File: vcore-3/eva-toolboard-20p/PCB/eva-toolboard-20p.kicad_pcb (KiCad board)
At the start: 2 copper layers, 44.1 x 48.8 mm, 12 parts, among them J4 Main connector

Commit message: Added totally useless but cute logos
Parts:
- added svg2mod: G***, logos:EVA_Logo, F.Cu at (144.8, 99.3)
- added svg2mod: G***, logos:Jevermeister_Logo, F.Cu at (150.9, 99.8)
- added svg2mod: G***, logos:Heart_Logo, F.Cu at (155.7, 100.5)
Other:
- board text added: "+"
- board text added: "="

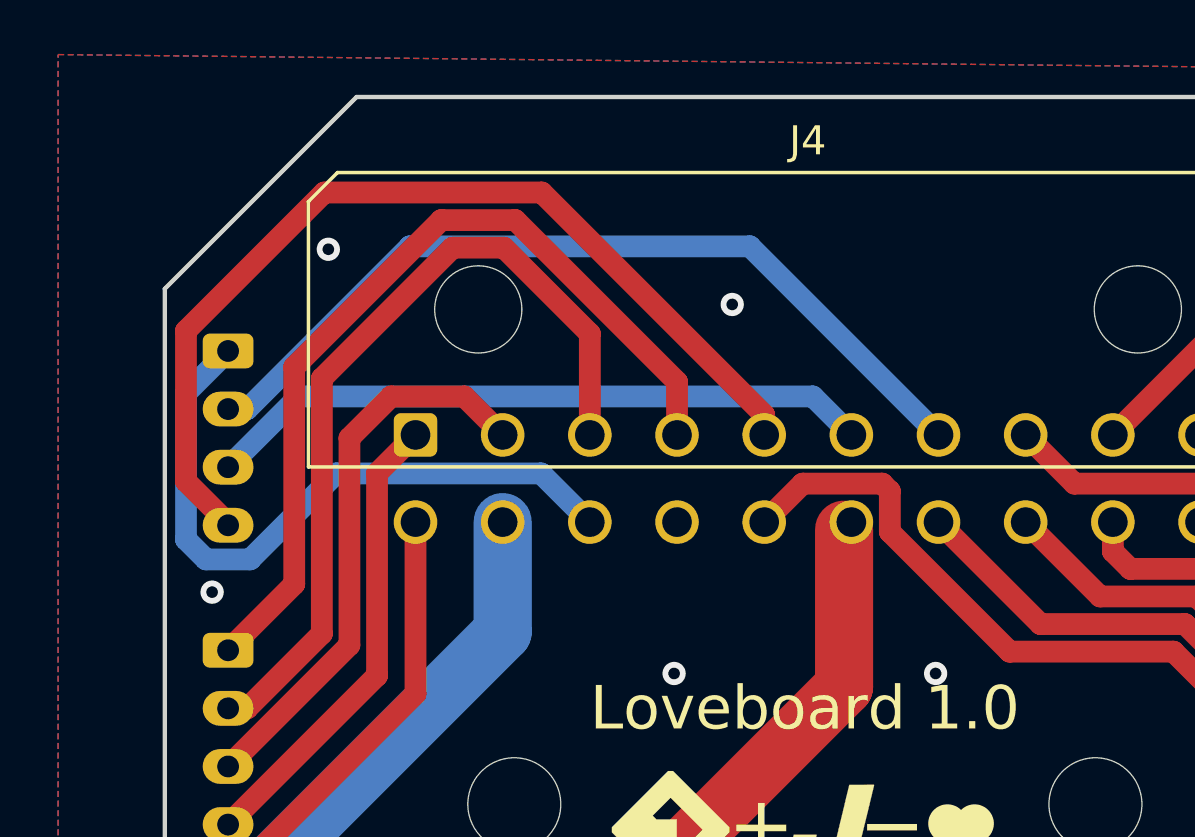
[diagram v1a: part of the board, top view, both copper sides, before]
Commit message: Beefed upper stepper tracks and some rerouting
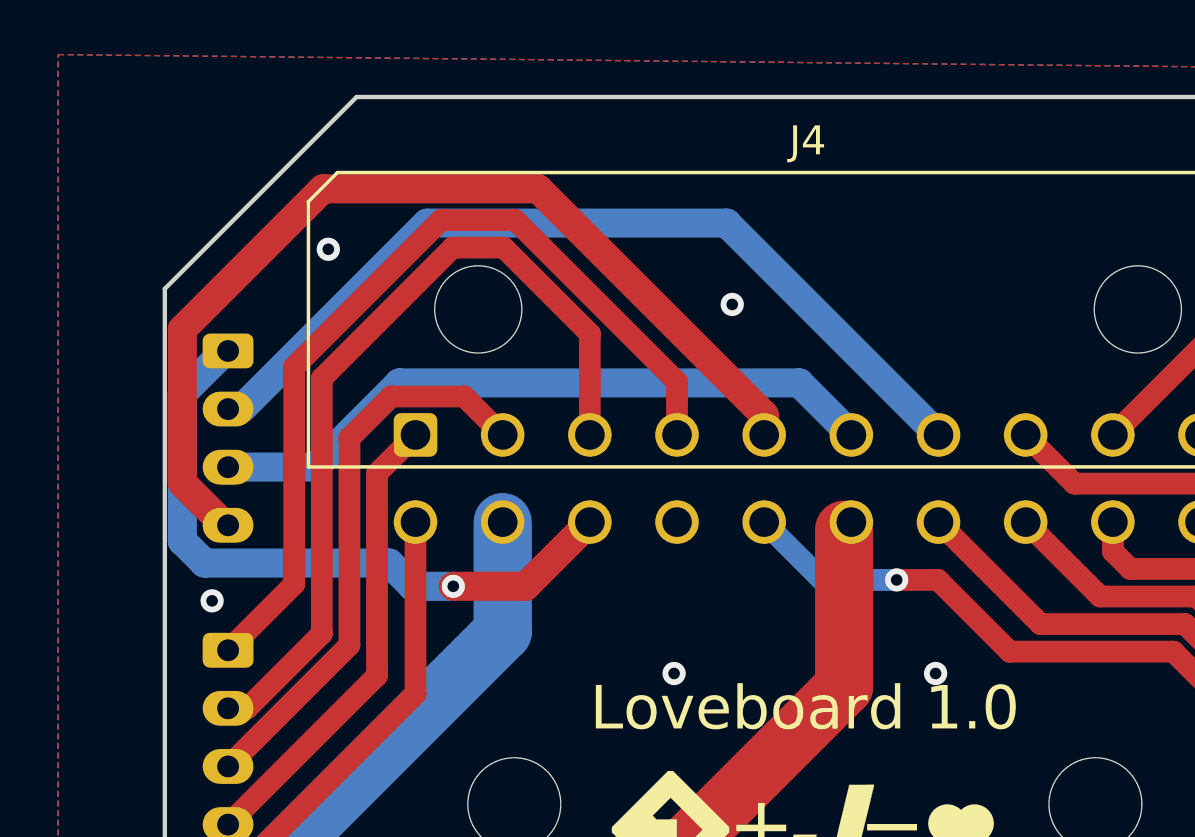
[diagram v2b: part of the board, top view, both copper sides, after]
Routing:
- net Net-(J4-Pad15): track 23.5 -> 21.6 mm, vias 0 -> 1
- net Net-(J3-Pad2): track 29.5 -> 30.1 mm
- net Net-(J4-Pad13): track 23.2 -> 22.8 mm, vias 0 -> 1
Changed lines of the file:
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@@
   (segment (start 132.65507 110.43) (end 130.67548 108.45041) (width 2) (layer "B.Cu") (net 6))
   (segment (start 130.67548 104.754615) (end 131.729615 103.70048) (width 2) (layer "B.Cu") (net 6))
-  (segment (start 132.307176 86.9) (end 137.907176 81.3) (width 0.75) (layer "B.Cu") (net 7))
-  (segment (start 149.61 81.3) (end 156.1 87.79) (width 0.75) (layer "B.Cu") (net 7))
-  (segment (start 137.907176 81.3) (end 149.61 81.3) (width 0.75) (layer "B.Cu") (net 7))
-  (segment (start 131.65 86.9) (end 132.307176 86.9) (width 0.75) (layer "B.Cu") (net 7))
-  (segment (start 134.084511 86.465489) (end 151.775489 86.465489) (width 0.75) (layer "B.Cu") (net 8))
-  (segment (start 131.65 88.9) (end 134.084511 86.465489) (width 0.75) (layer "B.Cu") (net 8))
-  (segment (start 151.775489 86.465489) (end 153.1 87.79) (width 0.75) (layer "B.Cu") (net 8))
-  (segment (start 134.962514 79.446439) (end 142.446439 79.446439) (width 0.75) (layer "F.Cu") (net 9))
-  (segment (start 131.65 90.9) (end 131.713978 90.9) (width 0.75) (layer "F.Cu") (net 9))
-  (segment (start 142.446439 79.446439) (end 150.1 87.1) (width 0.75) (layer "F.Cu") (net 9))
-  (segment (start 130.20048 89.386502) (end 130.20048 84.208473) (width 0.75) (layer "F.Cu") (net 9))
-  (segment (start 131.713978 90.9) (end 130.20048 89.386502) (width 0.75) (layer "F.Cu") (net 9))
-  (segment (start 150.1 87.1) (end 150.1 87.79) (width 0.75) (layer "F.Cu") (net 9))
-  (segment (start 130.20048 84.208473) (end 134.962514 79.446439) (width 0.75) (layer "F.Cu") (net 9))
+  (segment (start 148.81 80.5) (end 156.1 87.79) (width 1) (layer "B.Cu") (net 7))
+  (segment (start 132.1 86.9) (end 138.5 80.5) (width 1) (layer "B.Cu") (net 7))
+  (segment (start 131.65 86.9) (end 132.1 86.9) (width 0.75) (layer "B.Cu") (net 7))
+  (segment (start 138.5 80.5) (end 148.81 80.5) (width 1) (layer "B.Cu") (net 7))
+  (segment (start 137.547177 86) (end 151.31 86) (width 1) (layer "B.Cu") (net 8))
+  (segment (start 134.647177 88.9) (end 137.547177 86) (width 1) (layer "B.Cu") (net 8))
+  (segment (start 131.65 88.9) (end 134.647177 88.9) (width 1) (layer "B.Cu") (net 8))
+  (segment (start 151.31 86) (end 153.1 87.79) (width 1) (layer "B.Cu") (net 8))
+  (segment (start 134.910736 79.32144) (end 142.32144 79.32144) (width 1) (layer "F.Cu") (net 9))
+  (segment (start 130.07548 84.156696) (end 134.910736 79.32144) (width 1) (layer "F.Cu") (net 9))
+  (segment (start 142.32144 79.32144) (end 150.1 87.1) (width 1) (layer "F.Cu") (net 9))
+  (segment (start 131.537202 90.9) (end 130.07548 89.438278) (width 1) (layer "F.Cu") (net 9))
+  (segment (start 150.1 87.1) (end 150.1 87.79) (width 1) (layer "F.Cu") (net 9))
+  (segment (start 130.07548 89.438278) (end 130.07548 84.156696) (width 1) (layer "F.Cu") (net 9))
   (segment (start 165.6 84.29) (end 162.1 87.79) (width 0.75) (layer "F.Cu") (net 10))
   (segment (start 171.4 84.29) (end 165.6 84.29) (width 0.75) (layer "F.Cu") (net 10))
   (via (at 135.1 81.4) (size 0.8) (drill 0.4) (layers "F.Cu" "B.Cu") (free) (net 11))
   (via (at 137 113) (size 0.8) (drill 0.4) (layers "F.Cu" "B.Cu") (free) (net 11))
-  (via (at 131.1 93.2) (size 0.8) (drill 0.4) (layers "F.Cu" "B.Cu") (free) (net 11))
+  (via (at 131.1 93.5) (size 0.8) (drill 0.4) (layers "F.Cu" "B.Cu") (free) (net 11))
   (via (at 156 96) (size 0.8) (drill 0.4) (layers "F.Cu" "B.Cu") (free) (net 11))
   (via (at 147 96) (size 0.8) (drill 0.4) (layers "F.Cu" "B.Cu") (free) (net 11))
   (via (at 149 83.3) (size 0.8) (drill 0.4) (layers "F.Cu" "B.Cu") (free) (net 11))
-  (segment (start 142.424511 89.114511) (end 144.1 90.79) (width 0.75) (layer "B.Cu") (net 12))
-  (segment (start 131.65 84.9) (end 130.20048 86.34952) (width 0.75) (layer "B.Cu") (net 12))
-  (segment (start 130.20048 86.34952) (end 130.20048 91.386502) (width 0.75) (layer "B.Cu") (net 12))
-  (segment (start 132.411502 92.07452) (end 135.371511 89.114511) (width 0.75) (layer "B.Cu") (net 12))
-  (segment (start 130.20048 91.386502) (end 130.888498 92.07452) (width 0.75) (layer "B.Cu") (net 12))
-  (segment (start 130.888498 92.07452) (end 132.411502 92.07452) (width 0.75) (layer "B.Cu") (net 12))
-  (segment (start 135.371511 89.114511) (end 142.424511 89.114511) (width 0.75) (layer "B.Cu") (net 12))
-  (segment (start 154.165489 89.465489) (end 151.424511 89.465489) (width 0.75) (layer "F.Cu") (net 14))
-  (segment (start 158.54856 95.24856) (end 154.424511 91.124511) (width 0.75) (layer "F.Cu") (net 14))
-  (segment (start 151.424511 89.465489) (end 150.1 90.79) (width 0.75) (layer "F.Cu") (net 14))
+  (segment (start 141.89 93) (end 144.1 90.79) (width 1) (layer "F.Cu") (net 12))
+  (segment (start 139.40048 93) (end 141.89 93) (width 1) (layer "F.Cu") (net 12))
+  (via (at 139.40048 93) (size 0.8) (drill 0.4) (layers "F.Cu" "B.Cu") (net 12))
+  (segment (start 130.07548 91.438278) (end 130.836722 92.19952) (width 1) (layer "B.Cu") (net 12))
+  (segment (start 130.836722 92.19952) (end 137.19952 92.19952) (width 1) (layer "B.Cu") (net 12))
+  (segment (start 130.07548 86.361722) (end 130.07548 91.438278) (width 1) (layer "B.Cu") (net 12))
+  (segment (start 137.19952 92.19952) (end 138 93) (width 1) (layer "B.Cu") (net 12))
+  (segment (start 131.65 84.9) (end 131.537202 84.9) (width 1) (layer "B.Cu") (net 12))
+  (segment (start 131.537202 84.9) (end 130.07548 86.361722) (width 1) (layer "B.Cu") (net 12))
+  (segment (start 138 93) (end 139.40048 93) (width 1) (layer "B.Cu") (net 12))
+  (segment (start 158.54856 95.24856) (end 156.1 92.8) (width 0.75) (layer "F.Cu") (net 14))
+  (segment (start 156.1 92.8) (end 156.08 92.78) (width 0.75) (layer "F.Cu") (net 14))
   (segment (start 167.25 99.6) (end 167.25 98.311296) (width 0.75) (layer "F.Cu") (net 14))
+  (segment (start 156.08 92.78) (end 154.66 92.78) (width 0.75) (layer "F.Cu") (net 14))
   (segment (start 167.25 98.311296) (end 164.187264 95.24856) (width 0.75) (layer "F.Cu") (net 14))
-  (segment (start 154.424511 89.724511) (end 154.165489 89.465489) (width 0.75) (layer "F.Cu") (net 14))
   (segment (start 164.187264 95.24856) (end 158.54856 95.24856) (width 0.75) (layer "F.Cu") (net 14))
-  (segment (start 154.424511 91.124511) (end 154.424511 89.724511) (width 0.75) (layer "F.Cu") (net 14))
+  (via (at 154.66 92.78) (size 0.8) (drill 0.4) (layers "F.Cu" "B.Cu") (net 14))
+  (segment (start 152.09 92.78) (end 150.1 90.79) (width 0.75) (layer "B.Cu") (net 14))
+  (segment (start 154.66 92.78) (end 152.09 92.78) (width 0.75) (layer "B.Cu") (net 14))
   (segment (start 159.60904 94.29904) (end 156.1 90.79) (width 0.75) (layer "F.Cu") (net 15))
   (segment (start 169.92644 104.37356) (end 169.92644 99.644912) (width 0.75) (layer "F.Cu") (net 15))

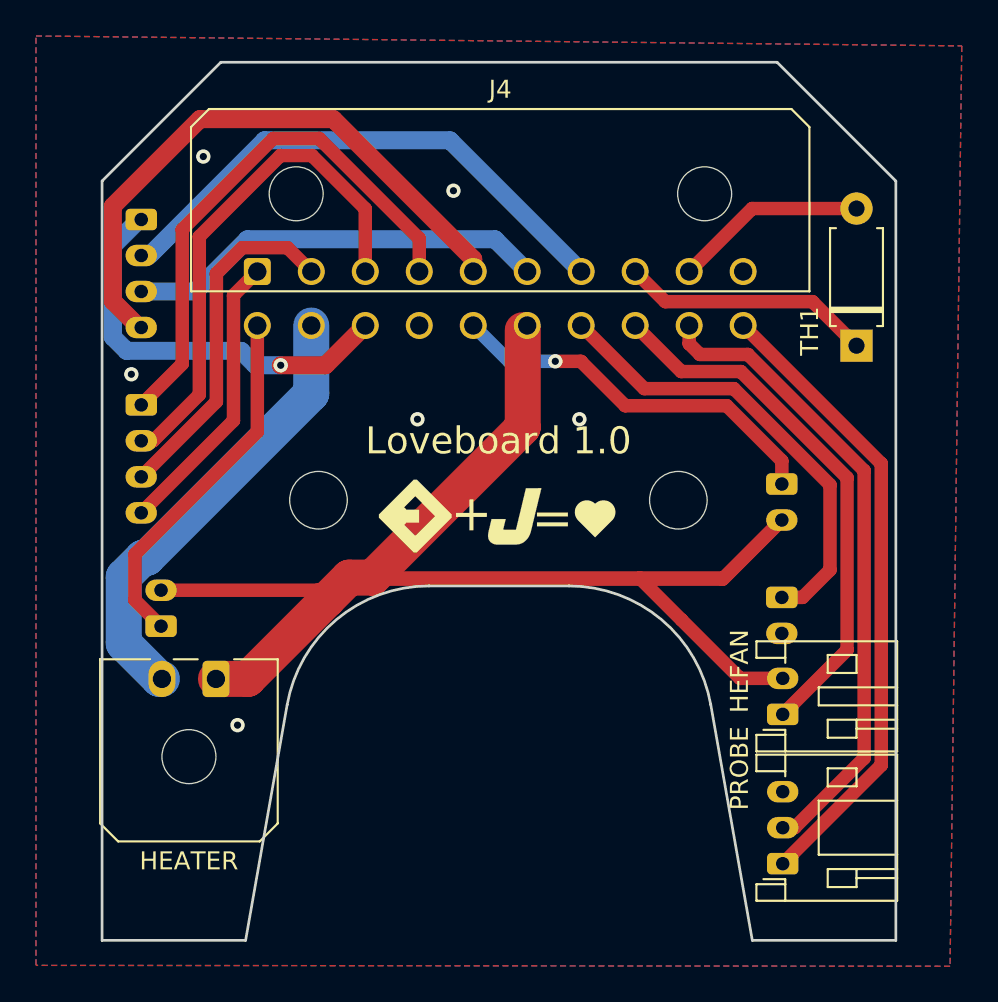
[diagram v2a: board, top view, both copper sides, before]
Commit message: Added Neopixel and unified part fan V-
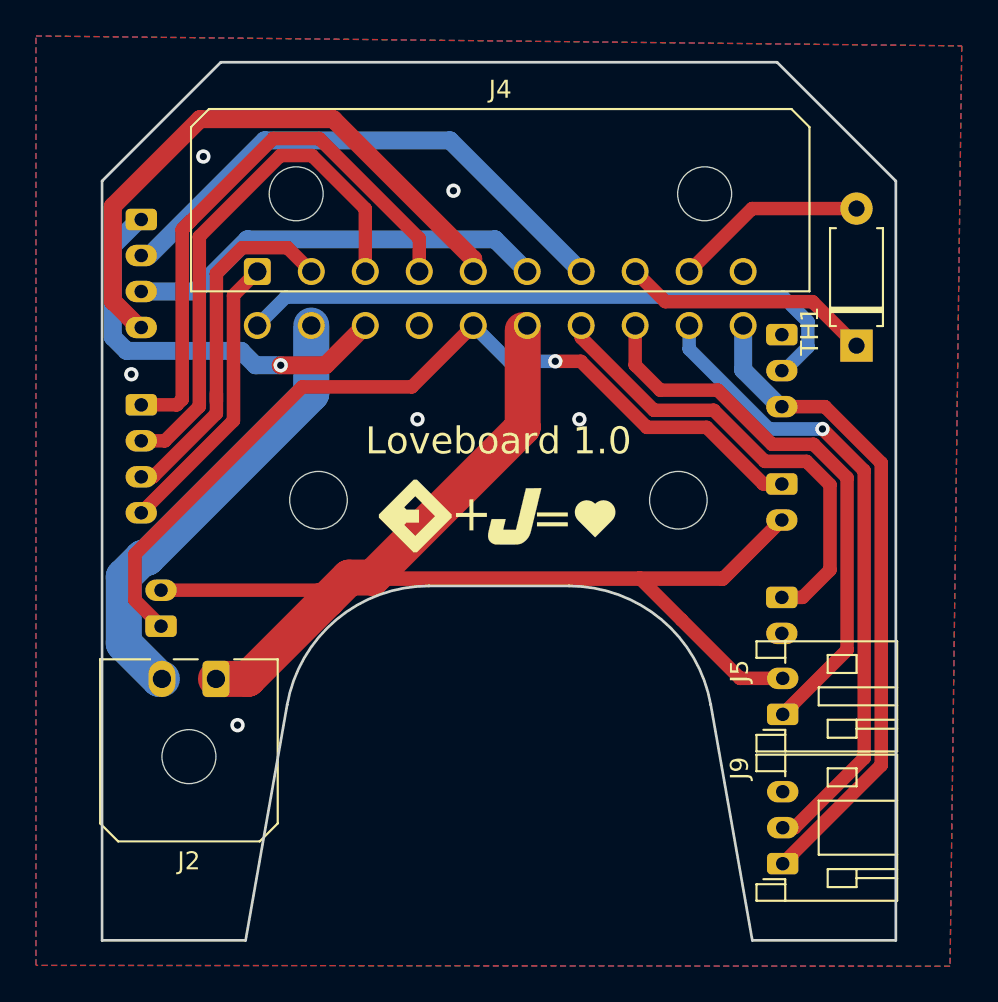
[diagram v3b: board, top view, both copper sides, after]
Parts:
- added J10: Neopixel, Connector_JST:JST_PH_S3B-PH-K_1x03_P2.00mm_Horizontal, B.Cu at (167.2, 91.3)
- renumbered TH0 to J1, HEATER to J2, STEPPER to J3, HEFAN to J5, PFAN1 to J6, PFAN2 to J7, E_X to J8, PROBE to J9
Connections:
- J4 pad 11: Net-(J7-Pad1) -> Net-(J4-Pad11)
- J7 pad 1: Net-(J7-Pad1) -> Net-(J4-Pad15)
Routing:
- net Net-(J4-Pad11): track 0.00 -> 35.2 mm
- net Net-(J4-Pad15): track 21.6 -> 49.5 mm
- net Net-(J7-Pad1): track 20.1 -> 0.00 mm
- net Net-(J1-Pad1): track 30.1 -> 31.9 mm
- net +5V: track 35.4 -> 36.8 mm
- net Net-(J4-Pad18): track 29.9 -> 31.2 mm
- net Net-(J1-Pad3): track 19.4 -> 20.3 mm
- net Net-(J4-Pad19): track 35.8 -> 35.9 mm, vias 0 -> 1
